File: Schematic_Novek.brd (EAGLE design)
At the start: 160 x 100 mm, 14 parts, among them IC1 STM32F10XCXT6

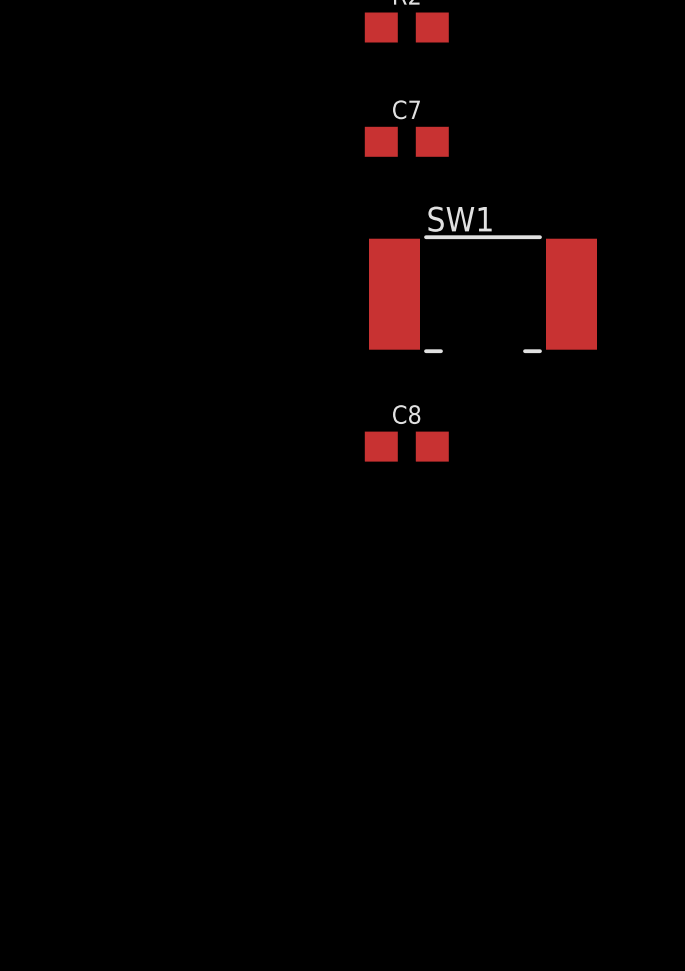
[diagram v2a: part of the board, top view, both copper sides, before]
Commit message: Adds header pin to switch between the different bootable memories
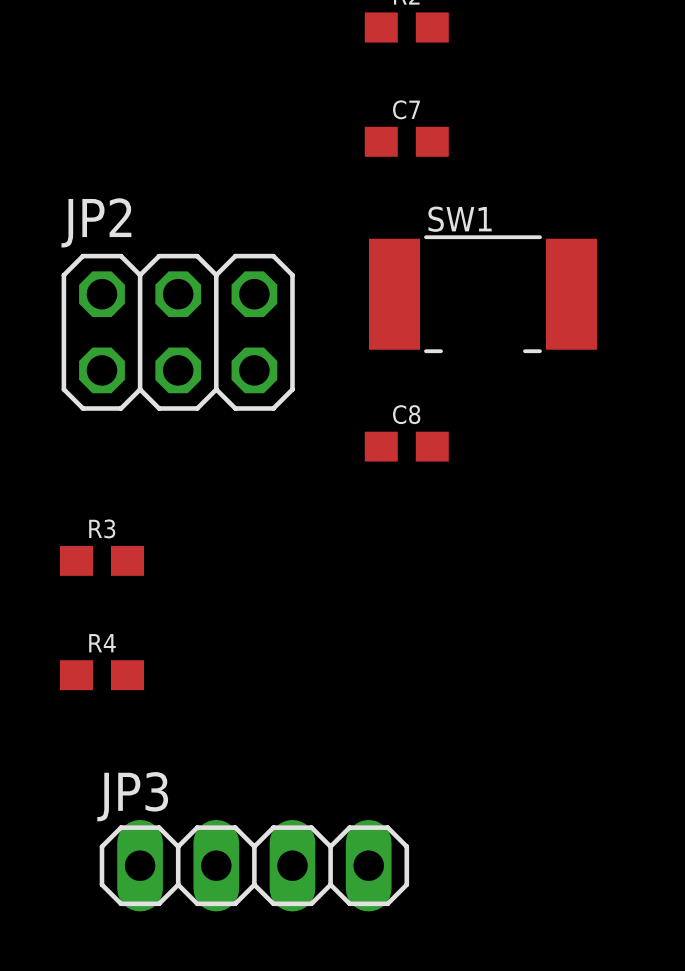
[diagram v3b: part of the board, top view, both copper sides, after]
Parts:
- added JP2: (no value), pinhead:2X03
- added JP3: (no value), pinhead:1X04
- added R3, R4: 100k, SparkFun-Resistors:0603
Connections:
- new net BOOT0: IC1.44, R3.1
- new net BOOT1: IC1.20, R4.2
- new net N$3: JP2.3, R3.2
- new net N$4: JP2.4, R4.1
- net 3.3V: now also JP2.1, JP2.2
- net GND: now also JP2.5, JP2.6
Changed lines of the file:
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@@
 <attribute name="VALUE" x="2.54" y="-75.692" size="0.6096" layer="27" font="vector" ratio="20" align="top-center"/>
+</element>
+<element name="JP2" library="pinhead" package="2X03" value="" x="-5.08" y="-71.12" smashed="yes">
+<attribute name="NAME" x="-8.89" y="-67.945" size="1.27" layer="25" ratio="10"/>
+<attribute name="VALUE" x="-8.89" y="-75.565" size="1.27" layer="27"/>
+</element>
+<element name="R3" library="SparkFun-Resistors" package="0603" value="100k" x="-7.62" y="-78.74" smashed="yes">
+<attribute name="NAME" x="-7.62" y="-77.978" size="0.6096" layer="25" font="vector" ratio="20" align="bottom-center"/>
+<attribute name="PROD_ID" value="RES-07828" x="-7.62" y="-78.74" size="1.778" layer="27" display="off"/>
+<attribute name="VALUE" x="-7.62" y="-79.502" size="0.6096" layer="27" font="vector" ratio="20" align="top-center"/>
+</element>
+<element name="R4" library="SparkFun-Resistors" package="0603" value="100k" x="-7.62" y="-82.55" smashed="yes">
+<attribute name="NAME" x="-7.62" y="-81.788" size="0.6096" layer="25" font="vector" ratio="20" align="bottom-center"/>
+<attribute name="PROD_ID" value="RES-07828" x="-7.62" y="-82.55" size="1.778" layer="27" display="off"/>
+<attribute name="VALUE" x="-7.62" y="-83.312" size="0.6096" layer="27" font="vector" ratio="20" align="top-center"/>
+</element>
+<element name="JP3" library="pinhead" library_urn="urn:adsk.eagle:library:325" package="1X04" package3d_urn="urn:adsk.eagle:package:22407/2" value="" x="-2.54" y="-88.9" smashed="yes">
+<attribute name="NAME" x="-7.6962" y="-87.0712" size="1.27" layer="25" ratio="10"/>
+<attribute name="POPULARITY" value="91" x="-2.54" y="-88.9" size="1.778" layer="27" display="off"/>
+<attribute name="VALUE" x="-7.62" y="-92.075" size="1.27" layer="27"/>
 </element>
 </elements>
@@
 <contactref element="JP1" pad="4"/>
 <contactref element="C8" pad="2"/>
+<contactref element="JP2" pad="5"/>
+<contactref element="JP2" pad="6"/>
+<wire x1="-2.54" y1="-69.85" x2="-2.54" y2="-72.39" width="0" layer="19" extent="1-1"/>
+<wire x1="3.39" y1="-74.93" x2="-2.54" y2="-72.39" width="0" layer="19" extent="1-1"/>
+<wire x1="1.69" y1="-64.77" x2="-2.54" y2="-69.85" width="0" layer="19" extent="1-1"/>
 <wire x1="8.03" y1="-69.85" x2="3.39" y2="-74.93" width="0" layer="19" extent="1-1"/>
-<wire x1="1.69" y1="-64.77" x2="8.03" y2="-69.85" width="0" layer="19" extent="1-1"/>
 <wire x1="3.39" y1="-57.15" x2="1.69" y2="-64.77" width="0" layer="19" extent="1-1"/>
 <wire x1="3.39" y1="-53.34" x2="3.39" y2="-57.15" width="0" layer="19" extent="1-1"/>
@@
 <contactref element="JP1" pad="1"/>
 <contactref element="C8" pad="1"/>
+<contactref element="JP2" pad="1"/>
+<contactref element="JP2" pad="2"/>
+<wire x1="-7.62" y1="-69.85" x2="-7.62" y2="-72.39" width="0" layer="19" extent="1-1"/>
+<wire x1="1.69" y1="-74.93" x2="-7.62" y2="-72.39" width="0" layer="19" extent="1-1"/>
 <wire x1="3.39" y1="-60.96" x2="1.69" y2="-74.93" width="0" layer="19" extent="1-1"/>
 <wire x1="1.69" y1="-57.15" x2="3.39" y2="-60.96" width="0" layer="19" extent="1-1"/>
@@
 <wire x1="4.6" y1="-1.85" x2="6.35" y2="-41.91" width="0" layer="19" extent="1-1"/>
 </signal>
+<signal name="N$3">
+<contactref element="R3" pad="2"/>
+<contactref element="JP2" pad="3"/>
+<wire x1="-5.08" y1="-72.39" x2="-6.77" y2="-78.74" width="0" layer="19" extent="1-1"/>
+</signal>
+<signal name="N$4">
+<contactref element="JP2" pad="4"/>
+<contactref element="R4" pad="1"/>
+<wire x1="-5.08" y1="-69.85" x2="-8.47" y2="-82.55" width="0" layer="19" extent="1-1"/>
+</signal>
+<signal name="BOOT0">
+<contactref element="IC1" pad="44"/>
+<contactref element="R3" pad="1"/>
+<wire x1="1.85" y1="-7.1" x2="-8.47" y2="-78.74" width="0" layer="19" extent="1-1"/>
+</signal>
+<signal name="BOOT1">
+<contactref element="IC1" pad="20"/>
+<contactref element="R4" pad="2"/>
+<wire x1="10.85" y1="-5.6" x2="-6.77" y2="-82.55" width="0" layer="19" extent="1-1"/>
+</signal>
 </signals>

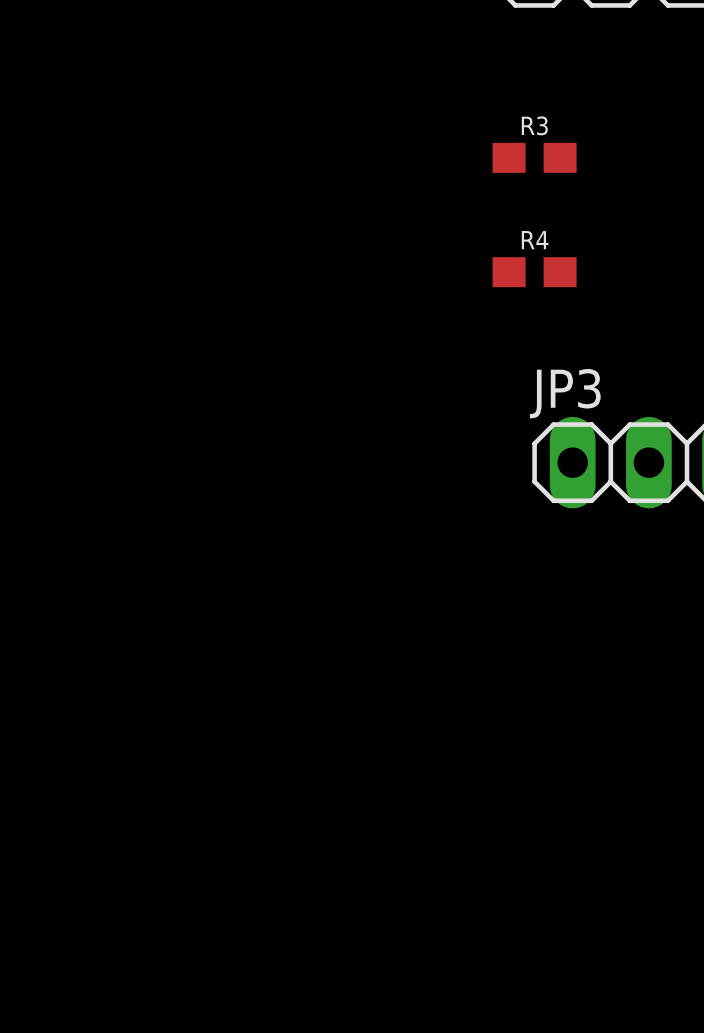
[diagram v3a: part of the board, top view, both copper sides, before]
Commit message: Adds bq21040
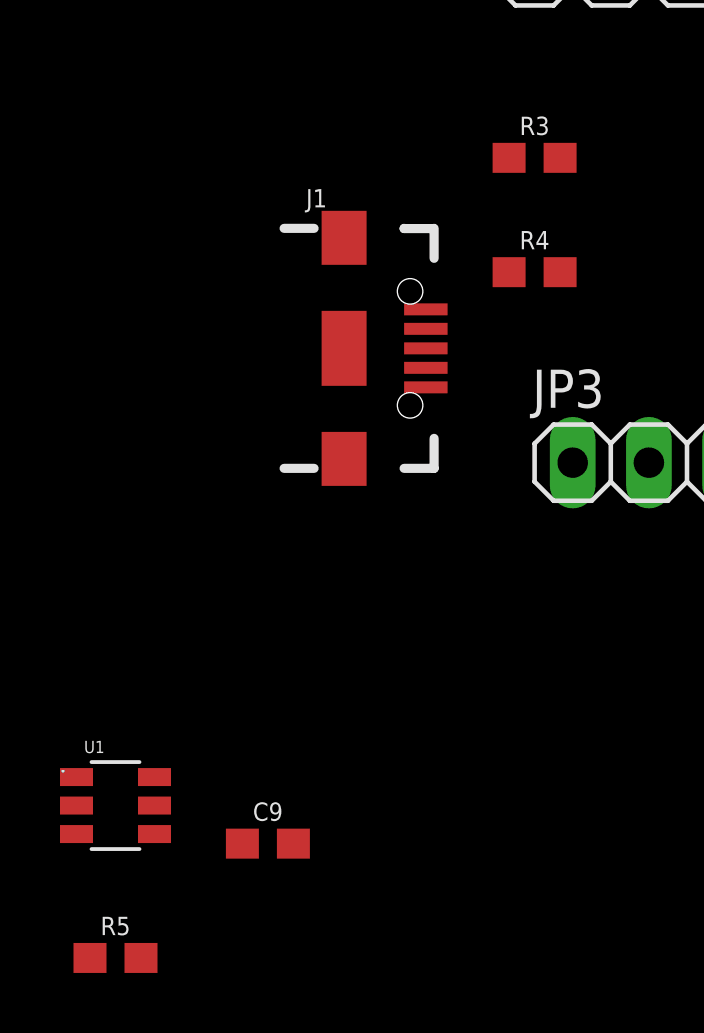
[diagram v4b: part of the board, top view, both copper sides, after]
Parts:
- added C9: 1.0uF, SparkFun-Capacitors:0603
- added J1: (no value), SparkFun-Connectors:USB-B-MICRO-SMD
- added R5: 1k, SparkFun-Resistors:0603
- added U1: BQ21040, bq21040:SOT23-6
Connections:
- new net 5V: JP3.3
- new net FTDI_RX: IC1.30, JP3.1
- new net FTDI_TX: IC1.31, JP3.2
- new net N$1: R5.2, U1.4
- new net VBUS: C9.2, J1.VBUS, U1.6
- new net VOUT: U1.2
- net GND: now also C9.1, J1.GND, J1.ID, JP3.4, R5.1, U1.5
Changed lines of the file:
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@@
 <attribute name="VALUE" x="-7.62" y="-92.075" size="1.27" layer="27"/>
+</element>
+<element name="J1" library="SparkFun-Connectors" package="USB-B-MICRO-SMD" value="" x="-13.97" y="-85.09" smashed="yes">
+<attribute name="NAME" x="-15.24" y="-80.391" size="0.6096" layer="25" font="vector" ratio="20"/>
+<attribute name="PROD_ID" value="CONN-11752" x="-13.97" y="-85.09" size="1.778" layer="27" display="off"/>
+<attribute name="VALUE" x="-15.24" y="-89.789" size="0.6096" layer="27" font="vector" ratio="20" align="top-left"/>
+</element>
+<element name="C9" library="SparkFun-Capacitors" package="0603" value="1.0uF" x="-16.51" y="-101.6" smashed="yes">
+<attribute name="NAME" x="-16.51" y="-100.838" size="0.6096" layer="25" font="vector" ratio="20" align="bottom-center"/>
+<attribute name="PROD_ID" value="CAP-00868" x="-16.51" y="-101.6" size="1.778" layer="27" display="off"/>
+<attribute name="VALUE" x="-16.51" y="-102.362" size="0.6096" layer="27" font="vector" ratio="20" align="top-center"/>
+</element>
+<element name="U1" library="bq21040" package="SOT23-6" value="BQ21040" x="-21.59" y="-100.33" smashed="yes">
+<attribute name="NAME" x="-22.64" y="-98.58" size="0.4064" layer="25"/>
+<attribute name="VALUE" x="-22.64" y="-102.48" size="0.4064" layer="27"/>
+</element>
+<element name="R5" library="SparkFun-Resistors" package="0603" value="1k" x="-21.59" y="-105.41" smashed="yes">
+<attribute name="NAME" x="-21.59" y="-104.648" size="0.6096" layer="25" font="vector" ratio="20" align="bottom-center"/>
+<attribute name="PROD_ID" value="RES-07856" x="-21.59" y="-105.41" size="1.778" layer="27" display="off"/>
+<attribute name="VALUE" x="-21.59" y="-106.172" size="0.6096" layer="27" font="vector" ratio="20" align="top-center"/>
 </element>
 </elements>
@@
 <contactref element="JP2" pad="5"/>
 <contactref element="JP2" pad="6"/>
+<contactref element="JP3" pad="4"/>
+<contactref element="J1" pad="GND"/>
+<contactref element="J1" pad="ID"/>
+<contactref element="C9" pad="1"/>
+<contactref element="U1" pad="5"/>
+<contactref element="R5" pad="1"/>
+<wire x1="-20.29" y1="-100.33" x2="-22.44" y2="-105.41" width="0" layer="19" extent="1-1"/>
+<wire x1="-17.36" y1="-101.6" x2="-20.29" y2="-100.33" width="0" layer="19" extent="1-1"/>
+<wire x1="-11.245" y1="-86.39" x2="-17.36" y2="-101.6" width="0" layer="19" extent="1-1"/>
+<wire x1="-11.245" y1="-85.74" x2="-11.245" y2="-86.39" width="0" layer="19" extent="1-1"/>
+<wire x1="1.27" y1="-88.9" x2="-11.245" y2="-86.39" width="0" layer="19" extent="1-1"/>
+<wire x1="3.39" y1="-74.93" x2="1.27" y2="-88.9" width="0" layer="19" extent="1-1"/>
+<wire x1="-2.54" y1="-72.39" x2="3.39" y2="-74.93" width="0" layer="19" extent="1-1"/>
 <wire x1="-2.54" y1="-69.85" x2="-2.54" y2="-72.39" width="0" layer="19" extent="1-1"/>
-<wire x1="3.39" y1="-74.93" x2="-2.54" y2="-72.39" width="0" layer="19" extent="1-1"/>
 <wire x1="1.69" y1="-64.77" x2="-2.54" y2="-69.85" width="0" layer="19" extent="1-1"/>
 <wire x1="8.03" y1="-69.85" x2="3.39" y2="-74.93" width="0" layer="19" extent="1-1"/>
@@
 <wire x1="10.85" y1="-5.6" x2="-6.77" y2="-82.55" width="0" layer="19" extent="1-1"/>
 </signal>
+<signal name="FTDI_RX">
+<contactref element="JP3" pad="1"/>
+<contactref element="IC1" pad="30"/>
+<wire x1="6.6" y1="-1.85" x2="-6.35" y2="-88.9" width="0" layer="19" extent="1-1"/>
+</signal>
+<signal name="FTDI_TX">
+<contactref element="JP3" pad="2"/>
+<contactref element="IC1" pad="31"/>
+<wire x1="6.1" y1="-1.85" x2="-3.81" y2="-88.9" width="0" layer="19" extent="1-1"/>
+</signal>
+<signal name="5V">
+<contactref element="JP3" pad="3"/>
+</signal>
+<signal name="VBUS">
+<contactref element="J1" pad="VBUS"/>
+<contactref element="U1" pad="6"/>
+<contactref element="C9" pad="2"/>
+<wire x1="-15.66" y1="-101.6" x2="-20.29" y2="-99.38" width="0" layer="19" extent="1-1"/>
+<wire x1="-11.245" y1="-83.79" x2="-20.29" y2="-99.38" width="0" layer="19" extent="1-1"/>
+</signal>
+<signal name="VOUT">
+<contactref element="U1" pad="2"/>
+</signal>
+<signal name="N$1">
+<contactref element="U1" pad="4"/>
+<contactref element="R5" pad="2"/>
+<wire x1="-20.29" y1="-101.28" x2="-20.74" y2="-105.41" width="0" layer="19" extent="1-1"/>
+</signal>
 </signals>
